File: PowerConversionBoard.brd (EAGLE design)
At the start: 152.4 x 101.6 mm, 48 parts, among them U1 LM2678, U2 LM2678

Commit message: ok
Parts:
- moved C15 0.77 mm to (17.7, 70.7)
- moved C16 0.69 mm to (24.2, 70.6)
- moved C17 0.60 mm to (30.6, 70.5)
- moved C18 0.58 mm to (37.1, 70.4)

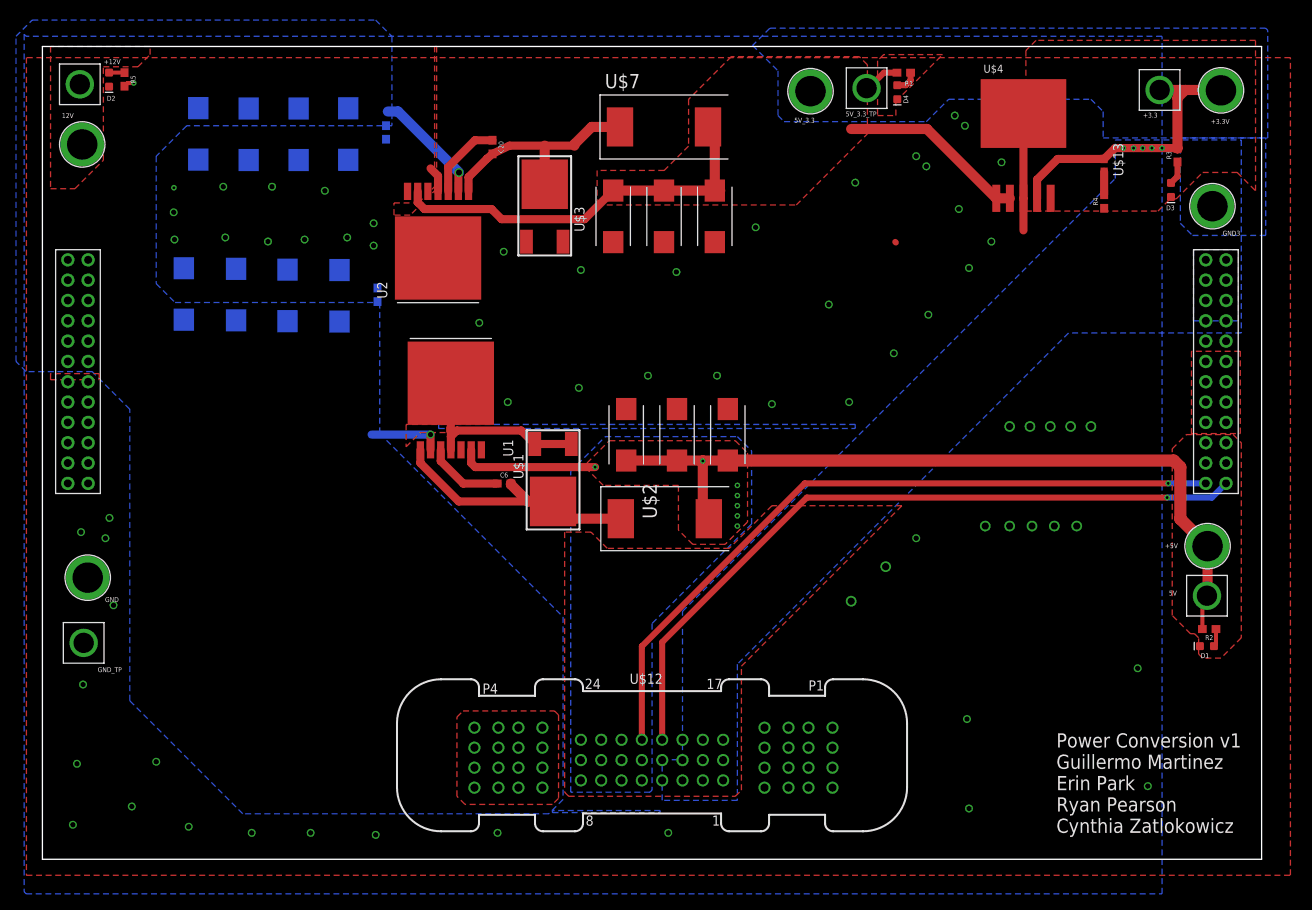
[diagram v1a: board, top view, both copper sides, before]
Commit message: CAD for connectors
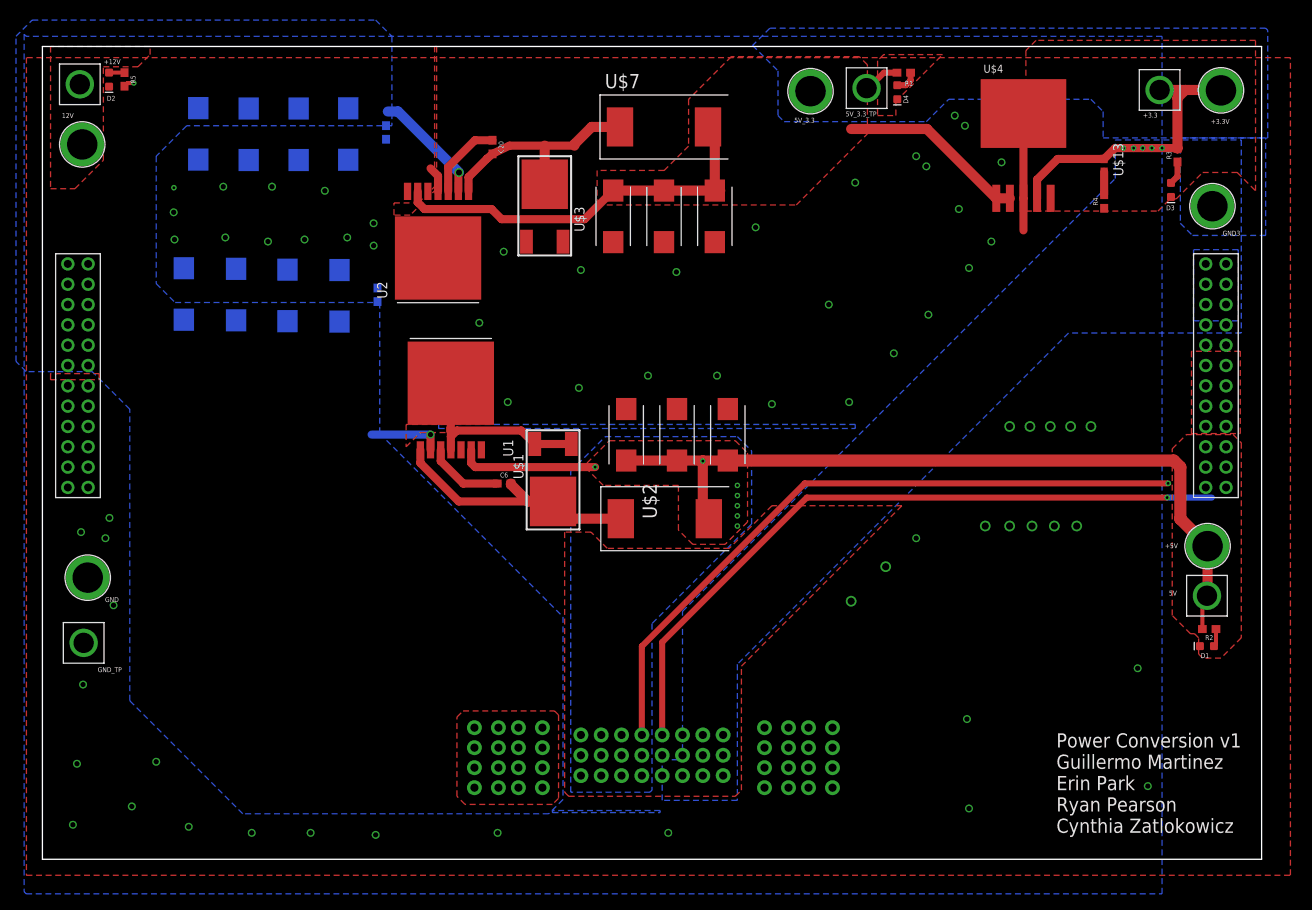
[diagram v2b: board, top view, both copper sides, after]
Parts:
- removed U$9: CONVERSION_TSW_12X2, Conversion_Connector:CONVERSION_TSW_12X2
- added U$5: CONVERSION_TSW_12X2, Dist_to_Conversion_Connector:CONVERSION_TSW_12X2
- flipped U$12 to the bottom, turned to 180 degrees
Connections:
- net +12V: now also U$5.1, U$5.10, U$5.11, U$5.12, U$5.2, U$5.3, U$5.4, U$5.5, U$5.6, U$5.7, U$5.8, U$5.9; no longer U$9.1, U$9.10, U$9.11, U$9.12, U$9.2, U$9.3, U$9.4, U$9.5, U$9.6, U$9.7, U$9.8, U$9.9
- net +3.3V: now also U$12.20, U$5.25, U$5.26, U$5.27, U$5.28, U$5.29, U$5.30, U$5.31, U$5.32; no longer U$12.4, U$9.25, U$9.26, U$9.27, U$9.28, U$9.29, U$9.30, U$9.31, U$9.32
- net +5V: now also U$12.21; no longer U$12.5
- net CAN_H: now also U$12.4, U$5.47; no longer U$12.20, U$9.47
- net CAN_L: now also U$12.5, U$5.48; no longer U$12.21, U$9.48
- net GND: now also U$5.13, U$5.14, U$5.15, U$5.16, U$5.17, U$5.18, U$5.19, U$5.20, U$5.21, U$5.22, U$5.23, U$5.24, U$5.35, U$5.36, U$5.37, U$5.38, U$5.39, U$5.40, U$5.41, U$5.42; no longer U$9.13, U$9.14, U$9.15, U$9.16, U$9.17, U$9.18, U$9.19, U$9.20, U$9.21, U$9.22, U$9.23, U$9.24, U$9.35, U$9.36, U$9.37, U$9.38, U$9.39, U$9.40, U$9.41, U$9.42
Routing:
- net CAN_L: track 90.6 -> 85.3 mm
- net CAN_H: track 90.9 -> 87.8 mm
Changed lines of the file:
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@@
 <?xml version="1.0" encoding="utf-8"?>
 <!DOCTYPE eagle SYSTEM "eagle.dtd">
-<eagle version="9.5.0">
+<eagle version="9.6.2">
 <drawing>
 <settings>
@@
 <setting verticaltext="up"/>
 </settings>
-<grid distance="1" unitdist="mil" unit="mil" style="lines" multiple="1" display="yes" altdistance="5" altunitdist="mil" altunit="inch"/>
+<grid distance="5" unitdist="mil" unit="mil" style="lines" multiple="1" display="yes" altdistance="5" altunitdist="mil" altunit="inch"/>
 <layers>
 <layer number="1" name="Top" color="4" fill="1" visible="yes" active="yes"/>
@@
 <attribute name="NAME" x="100.4062" y="92.8624" size="0.6096" layer="25"/>
 </element>
-<element name="U$12" library="ET60S-02-24-02-X-VP-GP" package="ET60S-02-24-02-X-VP-GP" value="ET60S-02-24-02-X-VP-GP" x="76.2" y="12.7" smashed="yes">
-<attribute name="NAME" x="73.4" y="21.935" size="1.27" layer="25"/>
-<attribute name="VALUE" x="73.908" y="24.801" size="1.27" layer="27"/>
+<element name="U$12" library="ET60S-02-24-02-X-VP-GP" package="ET60S-02-24-02-X-VP-GP" package3d_urn="urn:adsk.eagle:package:23038846/2" value="ET60S-02-24-02-X-VP-GP" x="76.2" y="12.7" smashed="yes" rot="MR180">
+<attribute name="NAME" x="73.4" y="3.465" size="1.27" layer="26" rot="MR180"/>
+<attribute name="VALUE" x="73.908" y="0.599" size="1.27" layer="28" rot="MR180"/>
 </element>
-<element name="U$9" library="Conversion_Connector" package="CONVERSION_TSW_12X2" value="CONVERSION_TSW_12X2" x="3.175" y="74.93" smashed="yes" rot="R270"/>
+<element name="U$5" library="Dist_to_Conversion_Connector" library_urn="urn:adsk.eagle:library:23140426" package="CONVERSION_TSW_12X2" package3d_urn="urn:adsk.eagle:package:23140429/2" value="CONVERSION_TSW_12X2" x="3.175" y="74.422" smashed="yes" rot="R270"/>
 </elements>
 <signals>
@@
 <contactref element="U2" pad="2"/>
 <contactref element="+12V" pad="P$1"/>
-<contactref element="U$9" pad="1"/>
-<contactref element="U$9" pad="11"/>
-<contactref element="U$9" pad="3"/>
-<contactref element="U$9" pad="5"/>
-<contactref element="U$9" pad="7"/>
-<contactref element="U$9" pad="9"/>
-<contactref element="U$9" pad="2"/>
-<contactref element="U$9" pad="12"/>
-<contactref element="U$9" pad="4"/>
-<contactref element="U$9" pad="6"/>
-<contactref element="U$9" pad="8"/>
-<contactref element="U$9" pad="10"/>
 <contactref element="U1" pad="2"/>
 <contactref element="C15" pad="+"/>
@@
 <vertex x="41.656" y="104.902"/>
 </polygon>
+<contactref element="U$5" pad="1"/>
+<contactref element="U$5" pad="3"/>
+<contactref element="U$5" pad="5"/>
+<contactref element="U$5" pad="7"/>
+<contactref element="U$5" pad="9"/>
+<contactref element="U$5" pad="11"/>
+<contactref element="U$5" pad="2"/>
+<contactref element="U$5" pad="12"/>
+<contactref element="U$5" pad="4"/>
+<contactref element="U$5" pad="6"/>
+<contactref element="U$5" pad="8"/>
+<contactref element="U$5" pad="10"/>
 </signal>
 <signal name="GND">
@@
 <via x="16.4338" y="83.947" extent="1-16" drill="0.35"/>
 <wire x1="84.0994" y1="77.0948" x2="84.0486" y2="77.1456" width="1.27" layer="1"/>
-<wire x1="106.68" y1="77.0948" x2="106.6038" y2="77.171" width="0.762" layer="1"/>
 <wire x1="122.6312" y1="82.6196" x2="122.6312" y2="78.613" width="1.016" layer="1"/>
 <wire x1="51.054" y1="59.9694" x2="51.054" y2="52.832" width="1.016" layer="1"/>
@@
 <wire x1="59.8594" y1="53.594" x2="51.816" y2="53.594" width="1.016" layer="1"/>
 <wire x1="66.1152" y1="51.9082" x2="61.5452" y2="51.9082" width="1.016" layer="1"/>
-<contactref element="U$9" pad="13"/>
-<contactref element="U$9" pad="23"/>
-<contactref element="U$9" pad="15"/>
-<contactref element="U$9" pad="17"/>
-<contactref element="U$9" pad="19"/>
-<contactref element="U$9" pad="21"/>
-<contactref element="U$9" pad="24"/>
-<contactref element="U$9" pad="14"/>
-<contactref element="U$9" pad="16"/>
-<contactref element="U$9" pad="18"/>
-<contactref element="U$9" pad="20"/>
-<contactref element="U$9" pad="22"/>
-<contactref element="U$9" pad="40"/>
-<contactref element="U$9" pad="36"/>
-<contactref element="U$9" pad="38"/>
-<contactref element="U$9" pad="41"/>
-<contactref element="U$9" pad="35"/>
-<contactref element="U$9" pad="37"/>
-<contactref element="U$9" pad="39"/>
 <polygon width="0.1524" layer="1">
 <vertex x="143.637" y="63.5"/>
@@
 <vertex x="156" y="100.206"/>
 </polygon>
-<contactref element="U$9" pad="42"/>
 <via x="120.904" y="54.102" extent="1-16" drill="0.9"/>
 <via x="123.444" y="54.102" extent="1-16" drill="0.9"/>
@@
 <via x="101.092" y="32.258" extent="1-16" drill="0.9"/>
 <via x="105.41" y="36.576" extent="1-16" drill="0.9"/>
+<contactref element="U$5" pad="13"/>
+<contactref element="U$5" pad="23"/>
+<contactref element="U$5" pad="21"/>
+<contactref element="U$5" pad="19"/>
+<contactref element="U$5" pad="17"/>
+<contactref element="U$5" pad="15"/>
+<contactref element="U$5" pad="14"/>
+<contactref element="U$5" pad="24"/>
+<contactref element="U$5" pad="16"/>
+<contactref element="U$5" pad="18"/>
+<contactref element="U$5" pad="20"/>
+<contactref element="U$5" pad="22"/>
+<contactref element="U$5" pad="35"/>
+<contactref element="U$5" pad="41"/>
+<contactref element="U$5" pad="37"/>
+<contactref element="U$5" pad="39"/>
+<contactref element="U$5" pad="36"/>
+<contactref element="U$5" pad="42"/>
+<contactref element="U$5" pad="38"/>
+<contactref element="U$5" pad="40"/>
 </signal>
 <signal name="+5V">
@@
 <wire x1="69.088" y1="49.022" x2="54.102" y2="49.022" width="1.016" layer="1"/>
 <contactref element="U$12" pad="8"/>
-<contactref element="U$12" pad="5"/>
 <contactref element="U$12" pad="6"/>
 <contactref element="U$12" pad="7"/>
@@
 <wire x1="145.6436" y1="39.1414" x2="145.6436" y2="33.02" width="1.27" layer="1"/>
 <wire x1="145.6436" y1="33.02" x2="145.5674" y2="32.9438" width="1.27" layer="1"/>
+<contactref element="U$12" pad="21"/>
 </signal>
 <signal name="+3.3V">
@@
 <wire x1="147.3708" y1="96.1644" x2="147.32" y2="96.1136" width="1.27" layer="1"/>
 <wire x1="124.3312" y1="84.9612" x2="124.3312" y2="82.6196" width="1.016" layer="1"/>
-<contactref element="U$9" pad="26"/>
-<contactref element="U$9" pad="32"/>
-<contactref element="U$9" pad="28"/>
-<contactref element="U$9" pad="30"/>
-<contactref element="U$9" pad="25"/>
-<contactref element="U$9" pad="31"/>
-<contactref element="U$9" pad="27"/>
-<contactref element="U$9" pad="29"/>
 <polygon width="0.1524" layer="16">
 <vertex x="143.891" y="76.2"/>
@@
 </polygon>
 <contactref element="U$12" pad="1"/>
-<contactref element="U$12" pad="4"/>
 <contactref element="U$12" pad="2"/>
 <contactref element="U$12" pad="3"/>
@@
 <via x="136.398" y="88.9" extent="1-16" drill="0.35"/>
 <via x="139.954" y="88.9" extent="1-16" drill="0.35"/>
+<contactref element="U$12" pad="20"/>
+<contactref element="U$5" pad="25"/>
+<contactref element="U$5" pad="31"/>
+<contactref element="U$5" pad="27"/>
+<contactref element="U$5" pad="29"/>
+<contactref element="U$5" pad="26"/>
+<contactref element="U$5" pad="32"/>
+<contactref element="U$5" pad="28"/>
+<contactref element="U$5" pad="30"/>
 </signal>
 <signal name="N$2">
@@
 </signal>
 <signal name="CAN_H">
-<contactref element="U$9" pad="47"/>
-<contactref element="U$12" pad="20"/>
-<wire x1="147.955" y1="46.99" x2="146.177" y2="45.212" width="0.762" layer="16"/>
 <via x="140.589" y="45.212" extent="1-16" drill="0.35"/>
 <wire x1="140.589" y1="45.212" x2="95.55" y2="45.212" width="0.762" layer="1"/>
 <wire x1="95.55" y1="45.212" x2="77.47" y2="27.132" width="0.762" layer="1"/>
-<wire x1="77.47" y1="27.132" x2="77.47" y2="14.94" width="0.762" layer="1"/>
 <wire x1="146.177" y1="45.212" x2="140.589" y2="45.212" width="0.762" layer="16"/>
+<contactref element="U$12" pad="4"/>
+<wire x1="77.47" y1="27.132" x2="77.47" y2="15.54" width="0.762" layer="1"/>
+<contactref element="U$5" pad="47"/>
+<wire x1="146.177" y1="45.212" x2="147.955" y2="46.482" width="0" layer="19" extent="16-16"/>
 </signal>
 <signal name="CAN_L">
-<contactref element="U$9" pad="48"/>
-<contactref element="U$12" pad="21"/>
 <wire x1="95.296" y1="46.99" x2="74.93" y2="26.624" width="0.762" layer="1"/>
-<wire x1="74.93" y1="26.624" x2="74.93" y2="14.94" width="0.762" layer="1"/>
 <wire x1="140.716" y1="46.99" x2="95.296" y2="46.99" width="0.762" layer="1"/>
 <via x="140.716" y="46.99" extent="1-16" drill="0.35"/>
-<wire x1="145.415" y1="46.99" x2="140.716" y2="46.99" width="0.762" layer="16"/>
+<contactref element="U$12" pad="5"/>
+<wire x1="74.93" y1="26.624" x2="74.93" y2="15.54" width="0.762" layer="1"/>
+<contactref element="U$5" pad="48"/>
+<wire x1="140.716" y1="46.99" x2="145.415" y2="46.482" width="0" layer="19" extent="1-1"/>
 </signal>
 <signal name="GNDCUT">

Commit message: chopped off corners
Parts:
- removed U$7: HCM1305, HCM1305:HCM1305
- added U$6: HCMA1305, Inductor_15uH - hcma1305:HCMA1305
- U$2: value HCM1305 -> HCMA1305; device HCM1305:HCM1305 -> Inductor_15uH - hcma1305:HCMA1305
- moved U$2 1.37 mm to (77.1, 41.4), turned to 0 degrees
- moved U$12 0.64 mm to (76.2, 13.3)
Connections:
- net +5V: now also U$2.P$2; no longer U$2.2
- net +5V_3.3V: now also U$6.P$2; no longer U$7.2
- net N$1: now also U$2.P$1; no longer U$2.1
- net N$7: now also U$6.P$1; no longer U$7.1
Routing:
- net +3.3V: track 37.0 -> 51.5 mm, vias 5 -> 6
- net CAN_H: track 87.8 -> 91.7 mm, vias 1 -> 2
- net CAN_L: track 85.3 -> 88.9 mm, vias 1 -> 2
- net N$1: track 33.5 -> 36.6 mm
- net +5V: track 116.5 -> 115.4 mm
- net +5V_3.3V: track 78.4 -> 77.5 mm
- net GND: vias 67 -> 57
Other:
- board size 152.4 x 101.6 mm -> 152.4 x 97.2 mm
